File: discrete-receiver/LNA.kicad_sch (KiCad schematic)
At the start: 8 parts, among them U16 PSA4-5043_

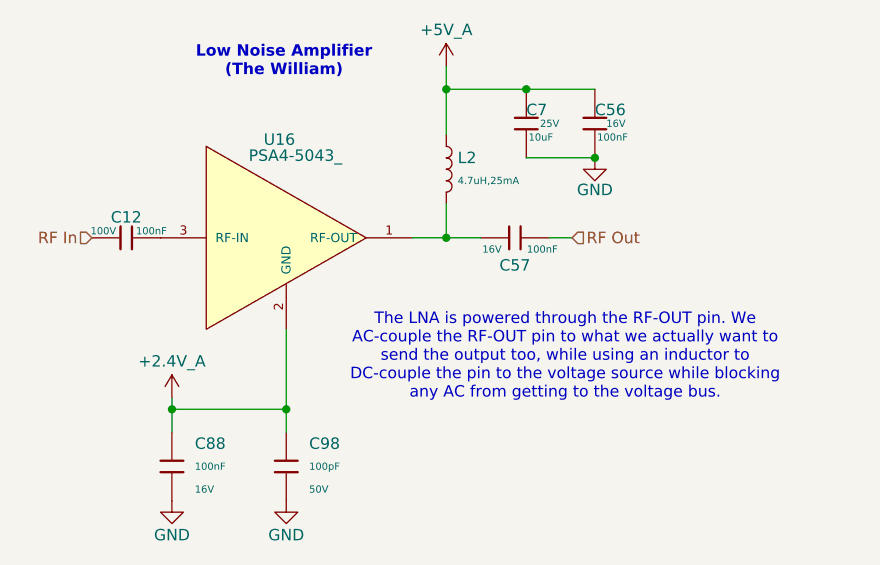
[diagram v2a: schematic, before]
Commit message: PCB Progress
Removed and replaced some residual +5V_A bus labels
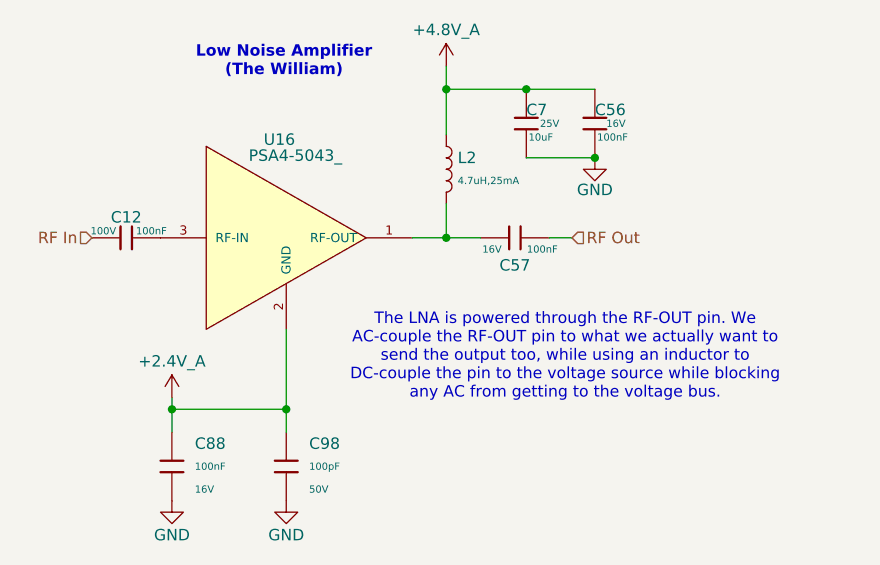
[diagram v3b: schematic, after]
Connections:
- net +5V_A renamed +4.8V_A
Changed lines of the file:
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@@
-	)
-	(symbol
-		(lib_id "power:+5V")
-		(at 147.32 82.55 0)
-		(unit 1)
-		(body_style 1)
-		(exclude_from_sim no)
-		(in_bom yes)
-		(on_board yes)
-		(in_pos_files yes)
-		(dnp no)
-		(property "Reference" "#PWR0123"
-			(at 147.32 86.36 0)
-			(hide yes)
-			(show_name no)
-			(do_not_autoplace no)
-			(effects
-				(font
-					(size 1.27 1.27)
-				)
-			)
-		)
-		(property "Value" "+5V_A"
-			(at 147.32 78.486 0)
-			(show_name no)
-			(do_not_autoplace no)
-			(effects
-				(font
-					(size 1.27 1.27)
-				)
-			)
-		)
-		(property "Footprint" ""
-			(at 147.32 82.55 0)
-			(hide yes)
-			(show_name no)
-			(do_not_autoplace no)
-			(effects
-				(font
-					(size 1.27 1.27)
-				)
-			)
-		)
-		(property "Datasheet" ""
-			(at 147.32 82.55 0)
-			(hide yes)
-			(show_name no)
-			(do_not_autoplace no)
-			(effects
-				(font
-					(size 1.27 1.27)
-				)
-			)
-		)
-		(property "Description" "Power symbol creates a global label with name \"+5V\""
-			(at 147.32 82.55 0)
-			(hide yes)
-			(show_name no)
-			(do_not_autoplace no)
-			(effects
-				(font
-					(size 1.27 1.27)
-				)
-			)
-		)
-		(pin "1"
-		)
-		(instances
-			(project "diode_tayloe_sdr"
-				(path "/d18d178d-3f10-4d68-9036-eae71a7d091a/c96fbd90-62d0-401a-a1f5-d4c4d983c9a4/0811a985-c39e-470e-b379-1c06ccf39cf9"
-					(reference "#PWR0123")
-					(unit 1)
-				)
-			)
-		)
 	)
 	(symbol
@@
 					(unit 1)
 				)
+			)
+		)
+	)
+	(symbol
+		(lib_id "power:+5V")
+		(at 147.32 82.55 0)
+		(unit 1)
+		(body_style 1)
+		(exclude_from_sim no)
+		(in_bom yes)
+		(on_board yes)
+		(in_pos_files yes)
+		(dnp no)
+		(property "Reference" "#PWR0123"
+			(at 147.32 86.36 0)
+			(hide yes)
+			(show_name no)
+			(do_not_autoplace no)
+			(effects
+				(font
+					(size 1.27 1.27)
+				)
+			)
+		)
+		(property "Value" "+4.8V_A"
+			(at 147.32 78.486 0)
+			(show_name no)
+			(do_not_autoplace no)
+			(effects
+				(font
+					(size 1.27 1.27)
+				)
+			)
+		)
+		(property "Footprint" ""
+			(at 147.32 82.55 0)
+			(hide yes)
+			(show_name no)
+			(do_not_autoplace no)
+			(effects
+				(font
+					(size 1.27 1.27)
+				)
+			)
+		)
+		(property "Datasheet" ""
+			(at 147.32 82.55 0)
+			(hide yes)
+			(show_name no)
+			(do_not_autoplace no)
+			(effects
+				(font
+					(size 1.27 1.27)
+				)
+			)
+		)
+		(property "Description" "Power symbol creates a global label with name \"+5V\""
+			(at 147.32 82.55 0)
+			(hide yes)
+			(show_name no)
+			(do_not_autoplace no)
+			(effects
+				(font
+					(size 1.27 1.27)
+				)
+			)
+		)
+		(pin "1"
+		)
+		(instances
+			(project "diode_tayloe_sdr"
+				(path "/d18d178d-3f10-4d68-9036-eae71a7d091a/c96fbd90-62d0-401a-a1f5-d4c4d983c9a4/0811a985-c39e-470e-b379-1c06ccf39cf9"
+					(reference "#PWR0123")
+					(unit 1)
+				)

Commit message: Updated JLC part numbers because some parts were out of stock
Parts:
- U16: LCSC (none) -> C5240848
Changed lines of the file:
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@@
+			)
+		)
+		(property "LCSC" "C5240848"
+			(at 128.27 101.6 0)
+			(hide yes)
+			(show_name no)
+			(do_not_autoplace no)
+			(effects
+				(font
+					(size 1.27 1.27)
+				)
 			)
 		)

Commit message: Fixed PCB component rotation offsets
A few components needed to get a rotation offset for JLCPCB production. Also more silkscreen content was added.
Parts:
- U16: Rotation Offset (none) -> 270
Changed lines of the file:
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@@
+			)
+		)
+		(property "Rotation Offset" "270"
+			(at 128.27 101.6 0)
+			(hide yes)
+			(show_name no)
+			(do_not_autoplace no)
+			(effects
+				(font
+					(size 1.27 1.27)
+				)
 			)
 		)

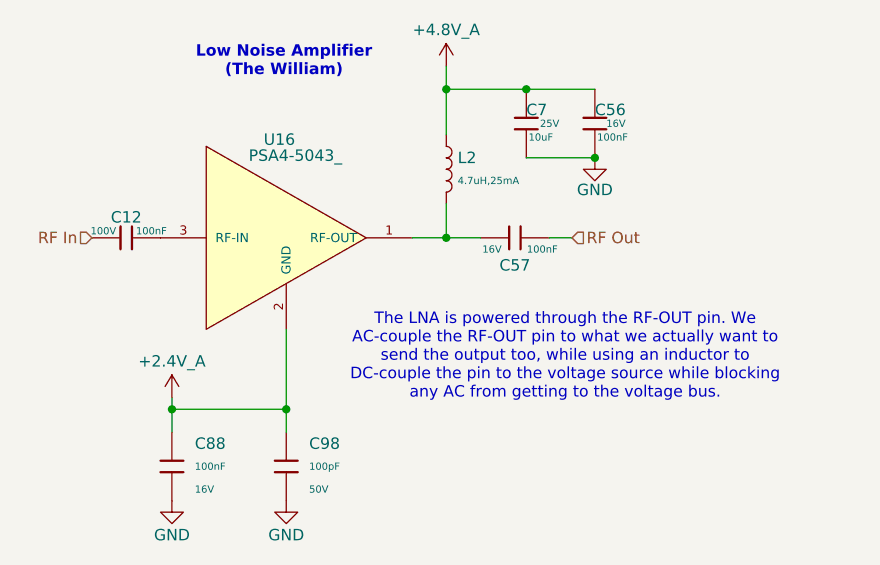
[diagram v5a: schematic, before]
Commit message: Schematic & PCB Edit
Removed C88 & C98 and the connection from the GND pin of the Low Noise Amplifier to +2.4V_A and instead tying it straight to GND.

Similarly removed C69 and C79 on T2 and tied T2 pin 4 to GND.
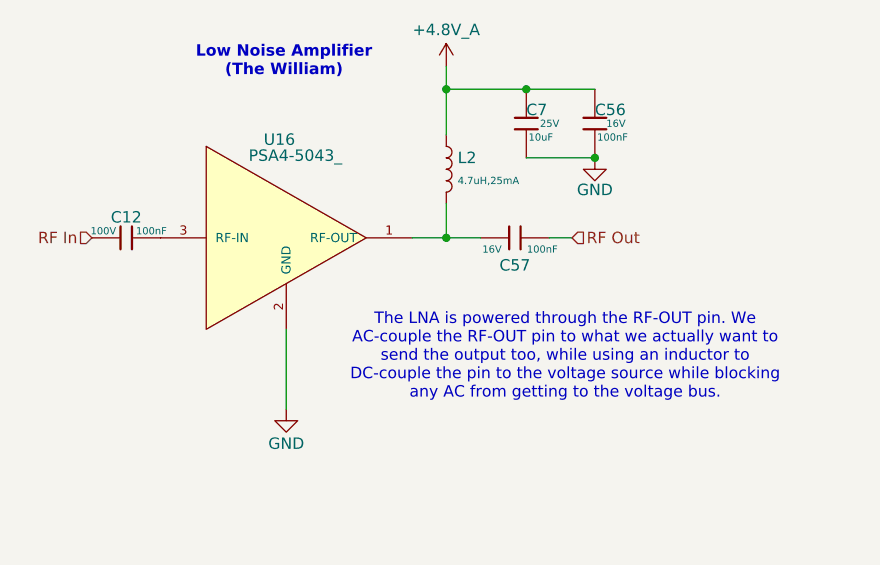
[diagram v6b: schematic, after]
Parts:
- removed C88: 100nF, PCM_JLCPCB:C_0402, symbol PCM_JLCPCB-Capacitors:0402,100nF
- removed C98: 100pF, PCM_JLCPCB:C_0603, symbol PCM_JLCPCB-Capacitors:0603,100pF
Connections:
- net +2.4V_A is gone; now on net GND: U16.2 (GND), U16.4 (GND__1)
